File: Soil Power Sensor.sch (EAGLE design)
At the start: 92 parts, among them IC1 TPD2E2U06DCK, J1 12401832E402A, U1 MAX9943ATT+, U10 FT234XD, U11 ESP32-C3-MINI-1-N4, U2 INA296A5, U3 THS4532, U4 FSA2466, U5 MAX11201A, U6 REF2033, U7 TLV1117LV33, U8 LM27761DSG, U9 WIO E5, X1 Voltage, X2 Current, X3 GND, X4 SDI, X5 SMA-142-0701-801/806

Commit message: Closes #2
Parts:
- removed C12, C17: 4.7uF, rcl:C-EUC0603
- removed C13, C14: NC, rcl:C-EUC0603
- removed C15, C16, C18: 0.1uF, rcl:C-EUC0603
- removed C7, C9: 1uF, rcl:C-EUC0603
- removed E1: MI0805K601R-10, Soil Power Sensor:MI0805K601R-10
- removed IC1: TPD2E2U06DCK, Soil Power Sensor:TPD2E2U06DCK
- removed J1: 12401832E402A, Connector_USB:12401832E402A
- removed R12, R15: 5.1k, rcl:R-US_R0603
- removed R16, R17, R18, R20, R21, R22, R23: 0, rcl:R-US_R0603
- removed S1: STM32 Reset, switch-omron:10-XX
- removed U10: FT234XD, Soil Power Sensor:FT234XD
- removed U9: WIO E5, Soil Power Sensor:WIO-E5
- removed X5: SMA-142-0701-801/806, con-coax:SMA-142-0701-801/806
- U7: value TLV1117LV33 -> WIO-E5_MINI; device Soil Power Sensor:TLV1117LV33 -> Soil Power Sensor:WIO-E5_MINI
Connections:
- removed net N$10: R20.1, U10.RTS
- removed net N$11: R21.1, U10.CTS
- removed net N$12: R22.1, U10.RXD
- removed net N$13: R23.1, U10.TXD
- removed net N$14: C18.1, U10.!RESET, U10.3V3OUT, U10.VCCIO
- removed net N$15: C16.1, C17.1, E1.2, U10.VCC
- removed net N$22: U9.PA0, X4-1.KL
- removed net N$6: J1.CC1, R12.2
- removed net N$7: J1.CC2, R15.1
- removed net PB6/TX: R23.2, U9.PB6
- removed net PB7/RX: R22.2, U9.PB7
- removed net STMR_D_N: R18.2, U10.USBDM
- removed net STMR_D_P: R17.2, U10.USBDP
- removed net STM_D_N: IC1.IO2, J1.D-1, J1.D-2, R18.1
- removed net STM_D_P: IC1.IO1, J1.D+1, J1.D+2, R17.1
- net +3V3: now also U7.3V3; no longer C12.1, C9.1, U7.OUT, U9.VCC
- net ESP32_EN: no longer U9.PA9
- net ESP32_RXD0: no longer U9.PA3
- net ESP32_TXD0: no longer U9.PA2
- net GND: no longer C12.2, C13.2, C14.2, C15.2, C16.2, C17.2, C18.2, C7.1, C9.2, IC1.GND, J1.GND1, J1.GND2, J1.GND3, J1.GND4, J1.SHIELD1, J1.SHIELD2, J1.SHIELD3, J1.SHIELD4, R12.1, R15.2, S1.S, S1.S1, U10.GND, U7.GND, U9.GND, U9.GND@1, U9.GND@2, U9.GND@3, X5.2
- net JTCK: no longer U9.PA14
- net JTDI: no longer U9.PA15
- net JTMS: no longer U9.PA13
- net N$2: now also U7.PA2/TX2, X4-1.KL; no longer C14.1, R16.2, X5.1
- net N$3: now also R13.1, R14.2; no longer C13.1, R16.1, U9.RFI0
- net N$34: now also U7.SCK/PB13; no longer R13.1, R14.2, U9.PA10
- net PB13/SPI2_SCK: no longer U9.PB13
- net PB14/SPI2_MISO: no longer U9.PB14
- net PB3/RTS/JTDO: no longer R20.2, U9.PB3
- net PB4/CTS/JNTRST: no longer R21.2, U9.PB4
- net PB9/SPI2_NSS: no longer U9.PB9
- net PC0: no longer U9.PC0
- net PC1: no longer U9.PC1
- net RST: no longer C15.1, S1.P, S1.P1, U9.RST
- net VCC: no longer C7.2, U7.IN
- net VUSB: now also U7.5V; no longer E1.1, J1.VBUS1, J1.VBUS2, J1.VBUS3, J1.VBUS4
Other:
- note removed: "0 Ohm resistors used for debugging"
- note removed: "1A Max Current Draw"
- note removed: "3V3 LDO"
- note removed: "5.1k resistors allow for 5V to be passed from host"
- note removed: "Capacitor for RST must be place as close as possible to the pin"
- note removed: "Ferite core placed somewhere between USB-C connector Vcc and FT234XD-R Vcc."
- note removed: "GNDs should be placed as close to components/pins as possible"
- note removed: "VDD_TCXO (Pin 28) must be left floating"
- moved on the sheet: R13, R14, X4-1, X4-2, X4-3

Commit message: Closes #3
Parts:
- removed C21, C22: NC, rcl:C-EUC0603
- removed JP4: STM32 JTAG, pinhead:PINHD-2X10
- removed JP5: ESP32 JTAG, pinhead:PINHD-2X10
- removed JP6: USB, jumper:JP1E
- removed R19, R27, R28: 0, rcl:R-US_R0603
- added D1, D2: ARM10_DEBUG, Soil Power Sensor:ARM10_DEBUG
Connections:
- removed net D_N: R27.1, U11.IO18
- removed net D_P: R28.1, U11.IO19
- removed net IO4/TMS: JP5.7, U11.IO4
- removed net IO5/TDI: JP5.5, U11.IO5
- removed net IO6/TCK: JP5.9, U11.IO6
- removed net IO7/TDO: JP5.13, U11.IO7
- removed net JTCK: JP4.9
- removed net JTDI: JP4.5
- removed net JTMS: JP4.7
- removed net N$39: C21.1, JP6.1, R27.2
- removed net N$40: C22.1, JP6.2, R28.2
- removed net NRST: JP4.15, R19.2
- removed net PB3/RTS/JTDO: JP4.13
- removed net PB4/CTS/JNTRST: JP4.3
- removed net RST: R19.1
- new net ESP32_TCK: D2.4, U11.IO6
- new net ESP32_TDI: D2.8, U11.IO5
- new net ESP32_TDO: D2.6, U11.IO7
- new net ESP32_TMS: D2.2, U11.IO4
- new net STM_SWDCLK: D1.4, U7.SWDLK/PA14
- new net STM_SWDIO: D1.2, U7.SWDIO/PA13
- new net STM_SWO: D1.6, U7.PB3/A3
- net +3V3: now also D1.1, D2.1; no longer JP4.1, JP4.2, JP5.1, JP5.2
- net ESP32_NRST: no longer JP5.15
- net GND: now also D1.3, D1.5, D1.9, D2.3, D2.5, D2.9; no longer C21.2, C22.2, JP4.10, JP4.12, JP4.14, JP4.16, JP4.18, JP4.20, JP4.4, JP4.6, JP4.8, JP5.10, JP5.12, JP5.14, JP5.16, JP5.18, JP5.20, JP5.4, JP5.6, JP5.8
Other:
- note removed: "Capacitors only placed if needed"
- note removed: "Resistor in case NRST does not work as expected"

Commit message: Closes #7
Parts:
- removed IN, IP, VBUF, VCM, VN, VP: TPB1,27, testpad:TPB1,27
- added -3V3, 3V3, REF_1V65, REF_3V3, VBAT, VCC, VUSB: TPB1,27, testpad:TPB1,27
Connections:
- net +3V3: now also 3V3.TP
- net -3V3: now also -3V3.TP
- net CURRENT_N: no longer IN.TP
- net CURRENT_P: no longer IP.TP
- net N$19: now also VBAT.TP
- net N$46: no longer VCM.TP
- net N$8: no longer VBUF.TP
- net REF+1V65: now also REF_1V65.TP
- net REF+3V3: now also REF_3V3.TP
- net VCC: now also VCC.TP
- net VOLTAGE_N: no longer VN.TP
- net VOLTAGE_P: no longer VP.TP
- net VUSB: now also VUSB.TP
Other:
- note added: "+3V3 comes from LDO on Wio-E5 mini"

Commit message: Closes #14
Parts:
- removed U1: MAX9943ATT+, Soil Power Sensor:MAX9943ATT+
- added U9: MAX9944ASA, Soil Power Sensor:MAX9944ASA
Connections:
- new net N$4: R3.1, U9B.-IN, U9B.OUT
- net +3V3: now also U9C.VCC; no longer U1.V+
- net -3V3: now also U9C.VEE; no longer U1.V-
- net N$1: now also U9A.+IN; no longer U1.+IN
- net N$46: now also U9B.+IN; no longer R3.1
- net N$8: now also U9A.-IN, U9A.OUT; no longer U1.-IN, U1.OUT
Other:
- moved on the sheet: R3, R9
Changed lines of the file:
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@@
 <part name="GND47" library="supply1" library_urn="urn:adsk.eagle:library:371" deviceset="GND" device=""/>
 <part name="U$3" library="Soil Power Sensor" deviceset="-3V3" device=""/>
-<part name="U1" library="Soil Power Sensor" deviceset="MAX9943" device="ATT+"/>
 <part name="U$1" library="Soil Power Sensor" deviceset="-3V3" device=""/>
 <part name="+3V9" library="Soil Power Sensor" deviceset="+3V3" device=""/>
@@
 <part name="REF_3V3" library="testpad" library_urn="urn:adsk.eagle:library:385" deviceset="TP" device="B1,27" package3d_urn="urn:adsk.eagle:package:27944/2"/>
 <part name="3V3" library="testpad" library_urn="urn:adsk.eagle:library:385" deviceset="TP" device="B1,27" package3d_urn="urn:adsk.eagle:package:27944/2"/>
+<part name="U9" library="Soil Power Sensor" deviceset="MAX9944" device="ASA"/>
 </parts>
 <sheets>
@@
 <plain>
 <text x="62.23" y="88.9" size="1.778" layer="94">G=200</text>
-<text x="124.46" y="142.24" size="1.778" layer="94">G=1</text>
+<text x="124.46" y="139.7" size="1.778" layer="94">G=1</text>
 <text x="114.3" y="55.88" size="1.778" layer="94">G=50</text>
 </plain>
@@
 <attribute name="MPN" x="106.68" y="193.04" size="1.778" layer="96" display="off"/>
 </instance>
-<instance part="R3" gate="G$1" x="106.68" y="152.4" smashed="yes">
-<attribute name="NAME" x="102.87" y="153.8986" size="1.778" layer="95"/>
-<attribute name="VALUE" x="102.87" y="149.098" size="1.778" layer="96"/>
-<attribute name="MPN" x="106.68" y="152.4" size="1.778" layer="96" display="off"/>
-</instance>
-<instance part="R9" gate="G$1" x="127" y="152.4" smashed="yes">
-<attribute name="NAME" x="123.19" y="153.8986" size="1.778" layer="95"/>
-<attribute name="VALUE" x="123.19" y="149.098" size="1.778" layer="96"/>
-<attribute name="MPN" x="127" y="152.4" size="1.778" layer="96" display="off"/>
+<instance part="R3" gate="G$1" x="106.68" y="149.86" smashed="yes">
+<attribute name="NAME" x="102.87" y="151.3586" size="1.778" layer="95"/>
+<attribute name="VALUE" x="102.87" y="146.558" size="1.778" layer="96"/>
+<attribute name="MPN" x="106.68" y="149.86" size="1.778" layer="96" display="off"/>
+</instance>
+<instance part="R9" gate="G$1" x="127" y="149.86" smashed="yes">
+<attribute name="NAME" x="123.19" y="151.3586" size="1.778" layer="95"/>
+<attribute name="VALUE" x="123.19" y="146.558" size="1.778" layer="96"/>
+<attribute name="MPN" x="127" y="149.86" size="1.778" layer="96" display="off"/>
 </instance>
 <instance part="R6" gate="G$1" x="124.46" y="104.14" smashed="yes">
@@
 <attribute name="NAME" x="181.61" y="52.578" size="1.778" layer="95"/>
 </instance>
-<instance part="U1" gate="A" x="55.88" y="193.04" smashed="yes">
-<attribute name="NAME" x="58.42" y="196.215" size="1.778" layer="95"/>
-<attribute name="VALUE" x="48.26" y="208.28" size="1.778" layer="96"/>
-</instance>
-<instance part="U$1" gate="A" x="55.88" y="182.88" smashed="yes" rot="R180">
-<attribute name="VALUE" x="53.34" y="180.34" size="1.778" layer="96"/>
-</instance>
-<instance part="+3V9" gate="G$1" x="55.88" y="203.2" smashed="yes">
-<attribute name="VALUE" x="58.42" y="205.74" size="1.778" layer="96" rot="R180"/>
+<instance part="U$1" gate="A" x="66.04" y="15.24" smashed="yes" rot="R180">
+<attribute name="VALUE" x="63.5" y="12.7" size="1.778" layer="96"/>
+</instance>
+<instance part="+3V9" gate="G$1" x="66.04" y="35.56" smashed="yes">
+<attribute name="VALUE" x="68.58" y="38.1" size="1.778" layer="96" rot="R180"/>
+</instance>
+<instance part="U9" gate="A" x="66.04" y="193.04" smashed="yes">
+<attribute name="NAME" x="63.5" y="199.39" size="1.778" layer="95"/>
+<attribute name="VALUE" x="67.31" y="196.85" size="1.778" layer="96"/>
+</instance>
+<instance part="U9" gate="B" x="66.04" y="149.86" smashed="yes">
+<attribute name="NAME" x="63.5" y="156.21" size="1.778" layer="95"/>
+<attribute name="VALUE" x="67.31" y="153.67" size="1.778" layer="96"/>
+</instance>
+<instance part="U9" gate="C" x="66.04" y="25.4" smashed="yes">
+<attribute name="NAME" x="62.23" y="24.638" size="1.778" layer="95"/>
 </instance>
 </instances>
@@
 </segment>
 <segment>
-<pinref part="U1" gate="A" pin="V+"/>
+<pinref part="U9" gate="C" pin="VCC"/>
 <pinref part="+3V9" gate="G$1" pin="+3V3"/>
 </segment>
@@
 <segment>
 <wire x1="114.3" y1="170.18" x2="116.84" y2="170.18" width="0.1524" layer="91"/>
-<wire x1="114.3" y1="152.4" x2="114.3" y2="170.18" width="0.1524" layer="91"/>
-<wire x1="111.76" y1="152.4" x2="114.3" y2="152.4" width="0.1524" layer="91"/>
+<wire x1="114.3" y1="149.86" x2="114.3" y2="170.18" width="0.1524" layer="91"/>
+<wire x1="111.76" y1="149.86" x2="114.3" y2="149.86" width="0.1524" layer="91"/>
 <pinref part="R3" gate="G$1" pin="2"/>
 <pinref part="R9" gate="G$1" pin="1"/>
-<wire x1="114.3" y1="152.4" x2="121.92" y2="152.4" width="0.1524" layer="91"/>
-<junction x="114.3" y="152.4"/>
+<wire x1="114.3" y1="149.86" x2="121.92" y2="149.86" width="0.1524" layer="91"/>
+<junction x="114.3" y="149.86"/>
 <pinref part="U3" gate="A" pin="-IN"/>
 </segment>
@@
 <pinref part="JP2" gate="-1" pin="2"/>
 <wire x1="25.4" y1="139.7" x2="27.94" y2="139.7" width="0.1524" layer="91"/>
-<pinref part="U1" gate="A" pin="+IN"/>
-<wire x1="48.26" y1="195.58" x2="27.94" y2="195.58" width="0.1524" layer="91"/>
+<wire x1="60.96" y1="195.58" x2="27.94" y2="195.58" width="0.1524" layer="91"/>
 <junction x="27.94" y="195.58"/>
+<pinref part="U9" gate="A" pin="+IN"/>
 </segment>
 </net>
@@
 <pinref part="X1" gate="-2" pin="KL"/>
 <wire x1="17.78" y1="190.5" x2="20.32" y2="190.5" width="0.1524" layer="91"/>
-<pinref part="R3" gate="G$1" pin="1"/>
-<wire x1="40.64" y1="152.4" x2="101.6" y2="152.4" width="0.1524" layer="91"/>
+<pinref part="U9" gate="B" pin="+IN"/>
+<wire x1="60.96" y1="152.4" x2="40.64" y2="152.4" width="0.1524" layer="91"/>
 <junction x="40.64" y="152.4"/>
 </segment>
@@
 <wire x1="154.94" y1="170.18" x2="170.18" y2="170.18" width="0.1524" layer="91"/>
 <pinref part="R9" gate="G$1" pin="2"/>
-<wire x1="132.08" y1="152.4" x2="137.16" y2="152.4" width="0.1524" layer="91"/>
-<wire x1="137.16" y1="152.4" x2="137.16" y2="170.18" width="0.1524" layer="91"/>
+<wire x1="132.08" y1="149.86" x2="137.16" y2="149.86" width="0.1524" layer="91"/>
+<wire x1="137.16" y1="149.86" x2="137.16" y2="170.18" width="0.1524" layer="91"/>
 <junction x="137.16" y="170.18"/>
 <pinref part="C2" gate="G$1" pin="1"/>
@@
 <net name="N$8" class="0">
 <segment>
-<pinref part="U1" gate="A" pin="-IN"/>
-<wire x1="48.26" y1="190.5" x2="45.72" y2="190.5" width="0.1524" layer="91"/>
-<wire x1="45.72" y1="190.5" x2="45.72" y2="177.8" width="0.1524" layer="91"/>
-<wire x1="45.72" y1="177.8" x2="66.04" y2="177.8" width="0.1524" layer="91"/>
-<wire x1="66.04" y1="177.8" x2="66.04" y2="193.04" width="0.1524" layer="91"/>
-<pinref part="U1" gate="A" pin="OUT"/>
-<wire x1="66.04" y1="193.04" x2="63.5" y2="193.04" width="0.1524" layer="91"/>
+<wire x1="58.42" y1="190.5" x2="58.42" y2="185.42" width="0.1524" layer="91"/>
+<wire x1="58.42" y1="185.42" x2="76.2" y2="185.42" width="0.1524" layer="91"/>
+<wire x1="76.2" y1="185.42" x2="76.2" y2="193.04" width="0.1524" layer="91"/>
+<wire x1="76.2" y1="193.04" x2="73.66" y2="193.04" width="0.1524" layer="91"/>
 <pinref part="R2" gate="G$1" pin="1"/>
-<wire x1="66.04" y1="193.04" x2="101.6" y2="193.04" width="0.1524" layer="91"/>
-<junction x="66.04" y="193.04"/>
+<wire x1="76.2" y1="193.04" x2="101.6" y2="193.04" width="0.1524" layer="91"/>
+<junction x="76.2" y="193.04"/>
+<pinref part="U9" gate="A" pin="OUT"/>
+<pinref part="U9" gate="A" pin="-IN"/>
+<wire x1="60.96" y1="190.5" x2="58.42" y2="190.5" width="0.1524" layer="91"/>
 </segment>
 </net>
 <net name="-3V3" class="0">
 <segment>
-<pinref part="U1" gate="A" pin="V-"/>
+<pinref part="U9" gate="C" pin="VEE"/>
 <pinref part="U$1" gate="A" pin="-3V3"/>
 </segment>
 </net>
+<net name="N$4" class="0">
+<segment>
+<pinref part="U9" gate="B" pin="-IN"/>
+<wire x1="60.96" y1="147.32" x2="58.42" y2="147.32" width="0.1524" layer="91"/>
+<wire x1="58.42" y1="147.32" x2="58.42" y2="142.24" width="0.1524" layer="91"/>
+<wire x1="58.42" y1="142.24" x2="76.2" y2="142.24" width="0.1524" layer="91"/>
+<wire x1="76.2" y1="142.24" x2="76.2" y2="149.86" width="0.1524" layer="91"/>
+<pinref part="U9" gate="B" pin="OUT"/>
+<wire x1="76.2" y1="149.86" x2="73.66" y2="149.86" width="0.1524" layer="91"/>
+<pinref part="R3" gate="G$1" pin="1"/>
+<wire x1="76.2" y1="149.86" x2="101.6" y2="149.86" width="0.1524" layer="91"/>
+<junction x="76.2" y="149.86"/>
+</segment>
+</net>

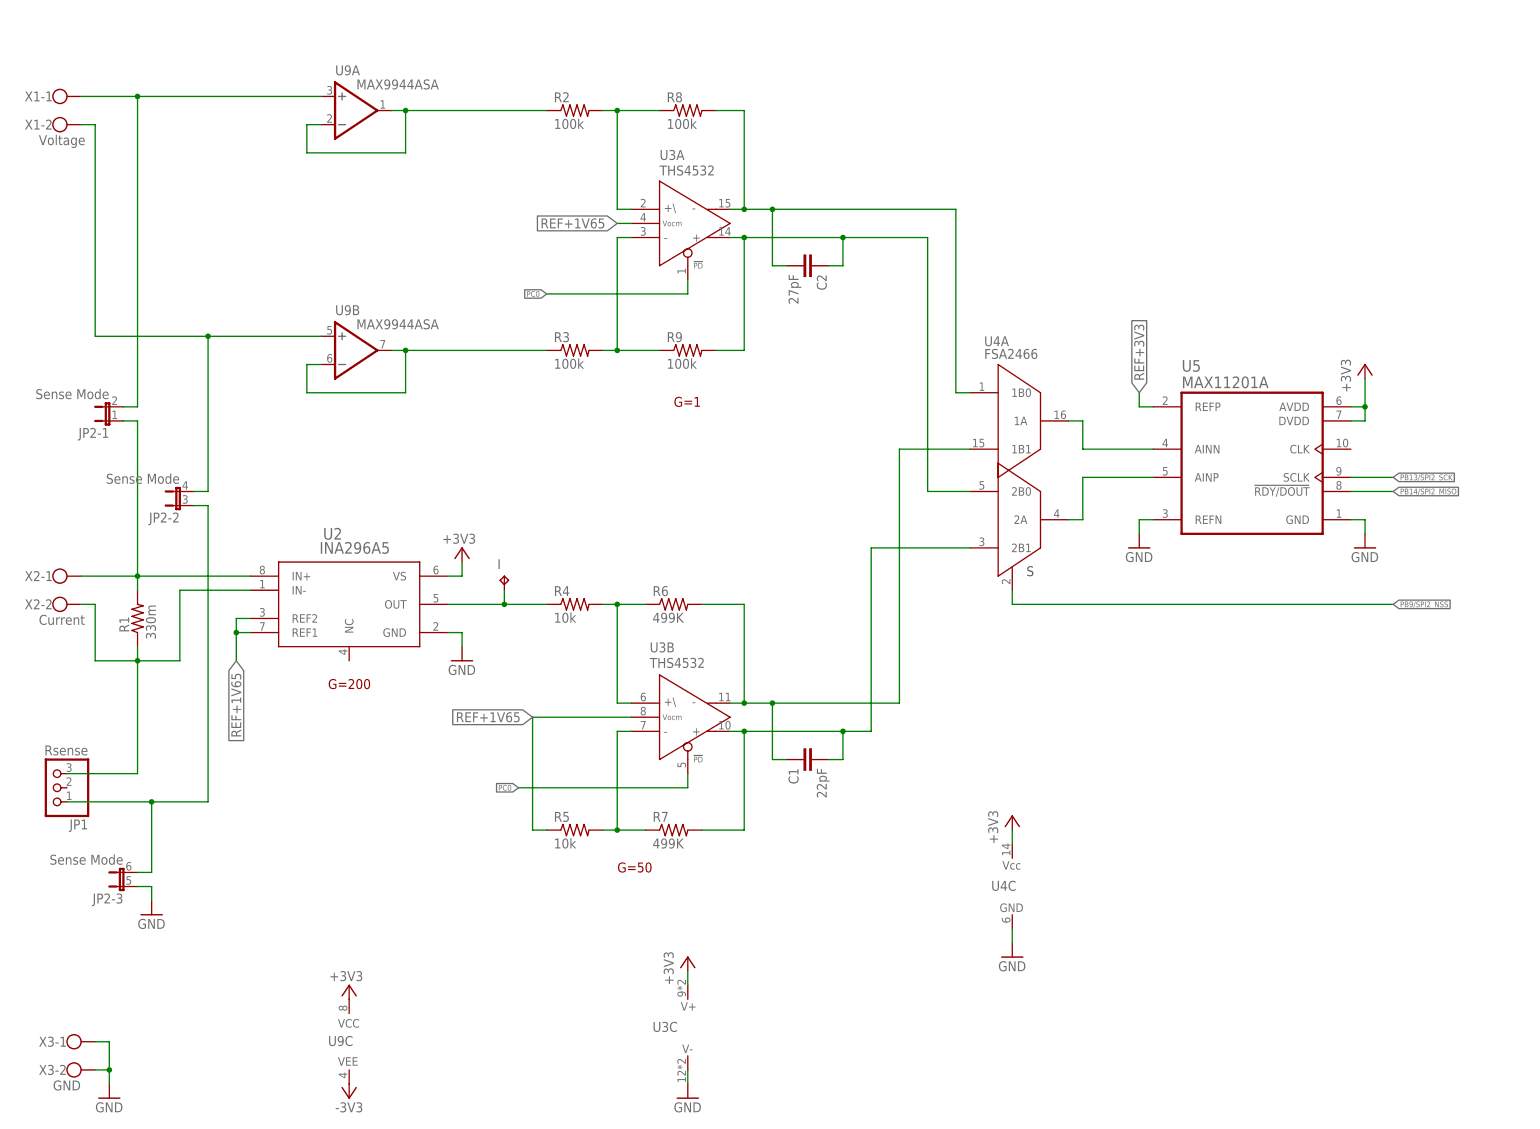
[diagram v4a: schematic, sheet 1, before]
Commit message: Closes #10
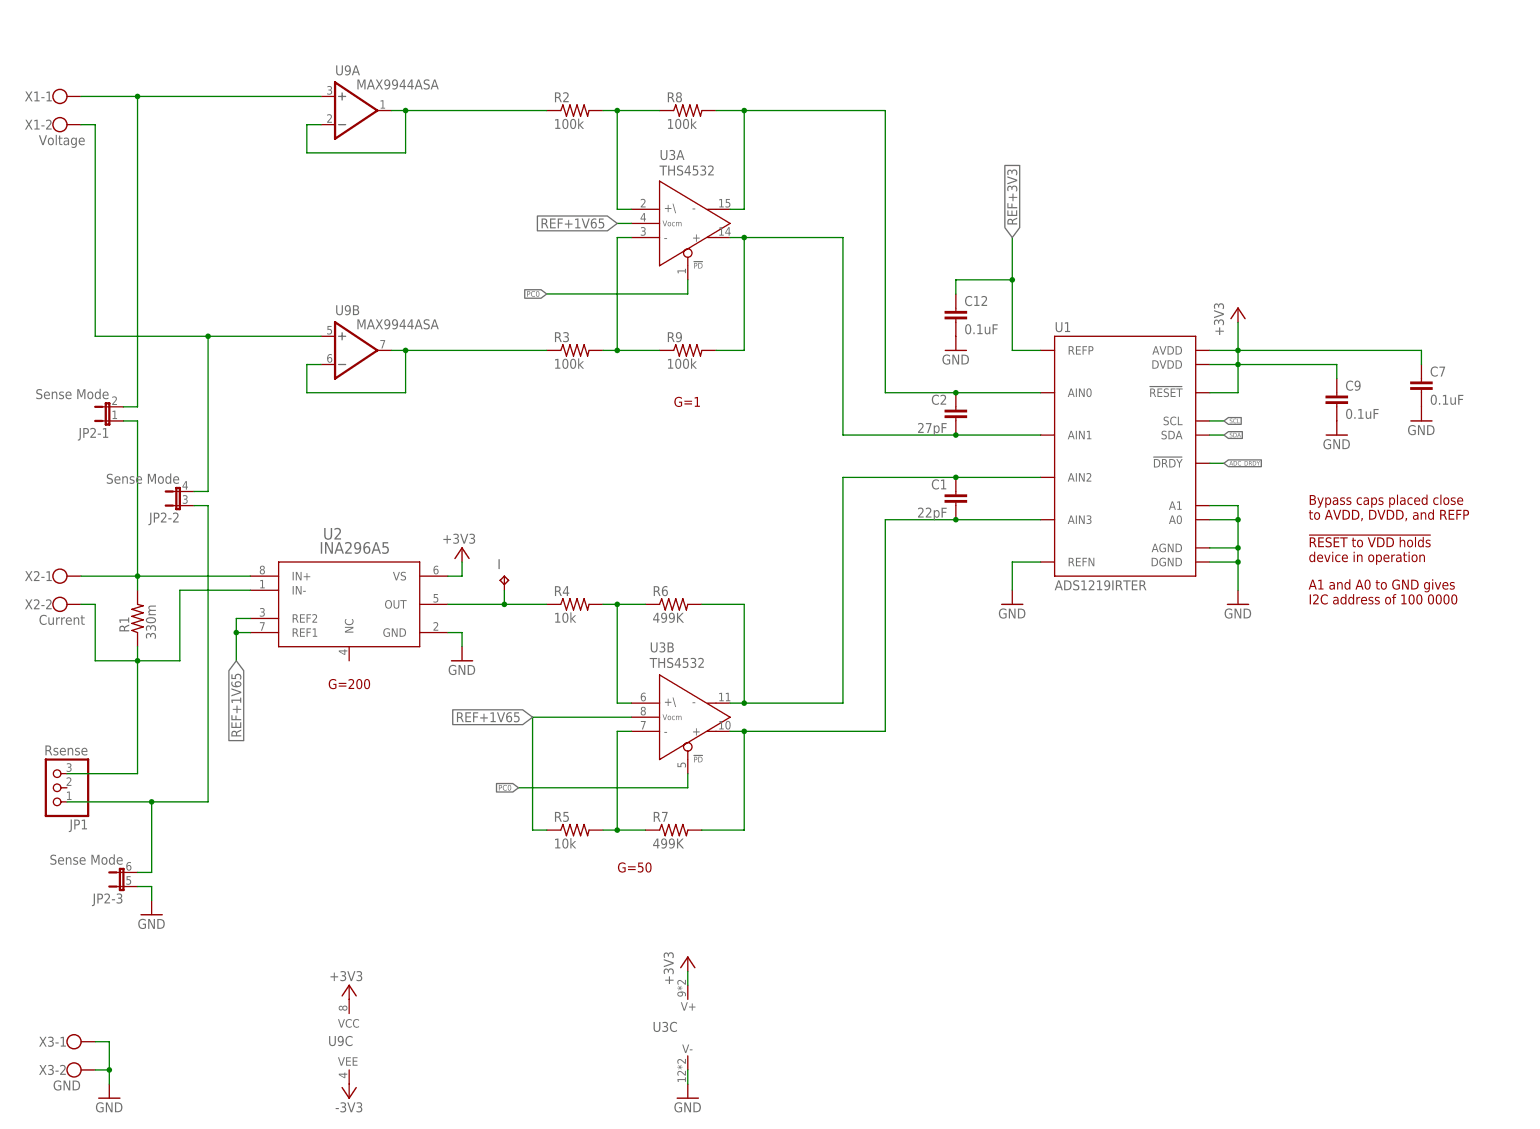
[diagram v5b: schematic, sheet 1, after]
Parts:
- removed U4: FSA2466, Soil Power Sensor:FSA2466
- removed U5: MAX11201A, Soil Power Sensor:MAX11201A
- added C12, C7, C9: 0.1uF, rcl:C-EUC0603
- added U1: ADS1219IRTER, Soil Power Sensor:ADS1219IRTER
- renumbered REF_1V65 to REF+1V65, REF_3V3 to REF+3V3
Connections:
- removed net CURRENT_N: C1.1, R6.2, U3B.OUT-, U4A.1B1
- removed net N$41: U4A.1A, U5.AINN
- removed net N$42: U4A.2A, U5.AINP
- removed net PB13/SPI2_SCK: U5.SCLK
- removed net PB14/SPI2_MISO: U5.!RDY/DOUT
- removed net PB9/SPI2_NSS: U4A.S
- new net ADC_DRDY: U1.!DRDY, U7.PA3/RX2
- new net N$9: C1.1, R6.2, U1.AIN2, U3B.OUT-
- new net SCL: U1.SCL, U7.PB15/SCL
- new net SDA: U1.SDA, U7.PA15/SDA
- net +3V3: now also C7.1, C9.1, U1.!RESET, U1.AVDD, U1.DVDD; no longer U4C.VCC, U5.AVDD, U5.DVDD
- net CURRENT_P: now also U1.AIN3; no longer U4A.2B1
- net GND: now also C12.2, C7.2, C9.2, U1.A0, U1.A1, U1.AGND, U1.DGND, U1.REFN; no longer U4C.GND, U5.GND, U5.REFN
- net REF+3V3: now also C12.1, U1.REFP; no longer U5.REFP
- net VOLTAGE_N: now also C2.1, U1.AIN0; no longer C2.2, U4A.1B0
- net VOLTAGE_P: now also C2.2, U1.AIN1; no longer C2.1, U4A.2B0
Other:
- note added: "!RESET to VDD holds device in operation"
- note added: "A1 and A0 to GND gives I2C address of 100 0000"
- note added: "Bypass caps placed close to AVDD, DVDD, and REFP"
- moved on the sheet: 3V3, C1, C2, R13, R14, U7
